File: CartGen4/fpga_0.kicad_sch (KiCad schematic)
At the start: 16 parts

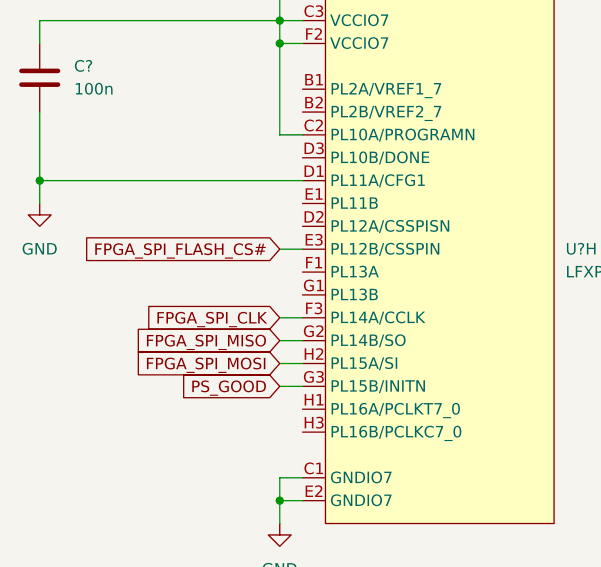
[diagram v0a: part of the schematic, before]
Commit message: Connected and fixed reset
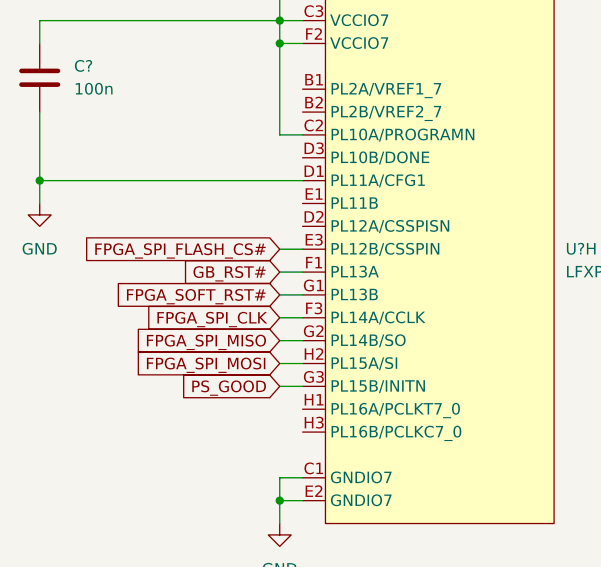
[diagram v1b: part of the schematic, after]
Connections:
- net GB_RST#: now reaches U?.F1 (PL13A)
- net FPGA_SOFT_RST#: now reaches U?.G1 (PL13B)
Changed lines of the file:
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@@
+    (stroke (width 0) (type default) (color 0 0 0 0))
+  )
+  (wire (pts (xy 53.34 74.93) (xy 55.88 74.93))
     (stroke (width 0) (type default) (color 0 0 0 0))
   )
@@
   )
   (wire (pts (xy 143.51 86.36) (xy 143.51 88.9))
+    (stroke (width 0) (type default) (color 0 0 0 0))
+  )
+  (wire (pts (xy 53.34 77.47) (xy 55.88 77.47))
     (stroke (width 0) (type default) (color 0 0 0 0))
   )
@@
     )
   )
+  (global_label "FPGA_SOFT_RST#" (shape input) (at 53.34 77.47 180) (fields_autoplaced)
+    (effects (font (size 1.27 1.27)) (justify right))
+    (property "Intersheet References" "${INTERSHEET_REFS}" (id 0) (at 34.9612 77.5494 0)
+      (effects (font (size 1.27 1.27)) (justify right) hide)
+    )
+  )
   (global_label "FPGA_SPI_CLK" (shape input) (at 53.34 80.01 180) (fields_autoplaced)
     (effects (font (size 1.27 1.27)) (justify right))
@@
       (effects (font (size 1.27 1.27)) (justify right) hide)
     )
+  )
+  (global_label "GB_RST#" (shape input) (at 53.34 74.93 180) (fields_autoplaced)
+    (effects (font (size 1.27 1.27)) (justify right))
+    (property "Intersheet References" "${INTERSHEET_REFS}" (id 0) (at 42.7021 75.0094 0)
+      (effects (font (size 1.27 1.27)) (justify right) hide)
+    )

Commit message: Added copyright
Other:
- company: (none) -> © Elijah Almeida Coimbra
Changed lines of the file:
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@@
   (title_block
     (title "FPGA connections 0")
+    (company "© Elijah Almeida Coimbra")
   )
   (junction (at 209.55 128.27) (diameter 0) (color 0 0 0 0)

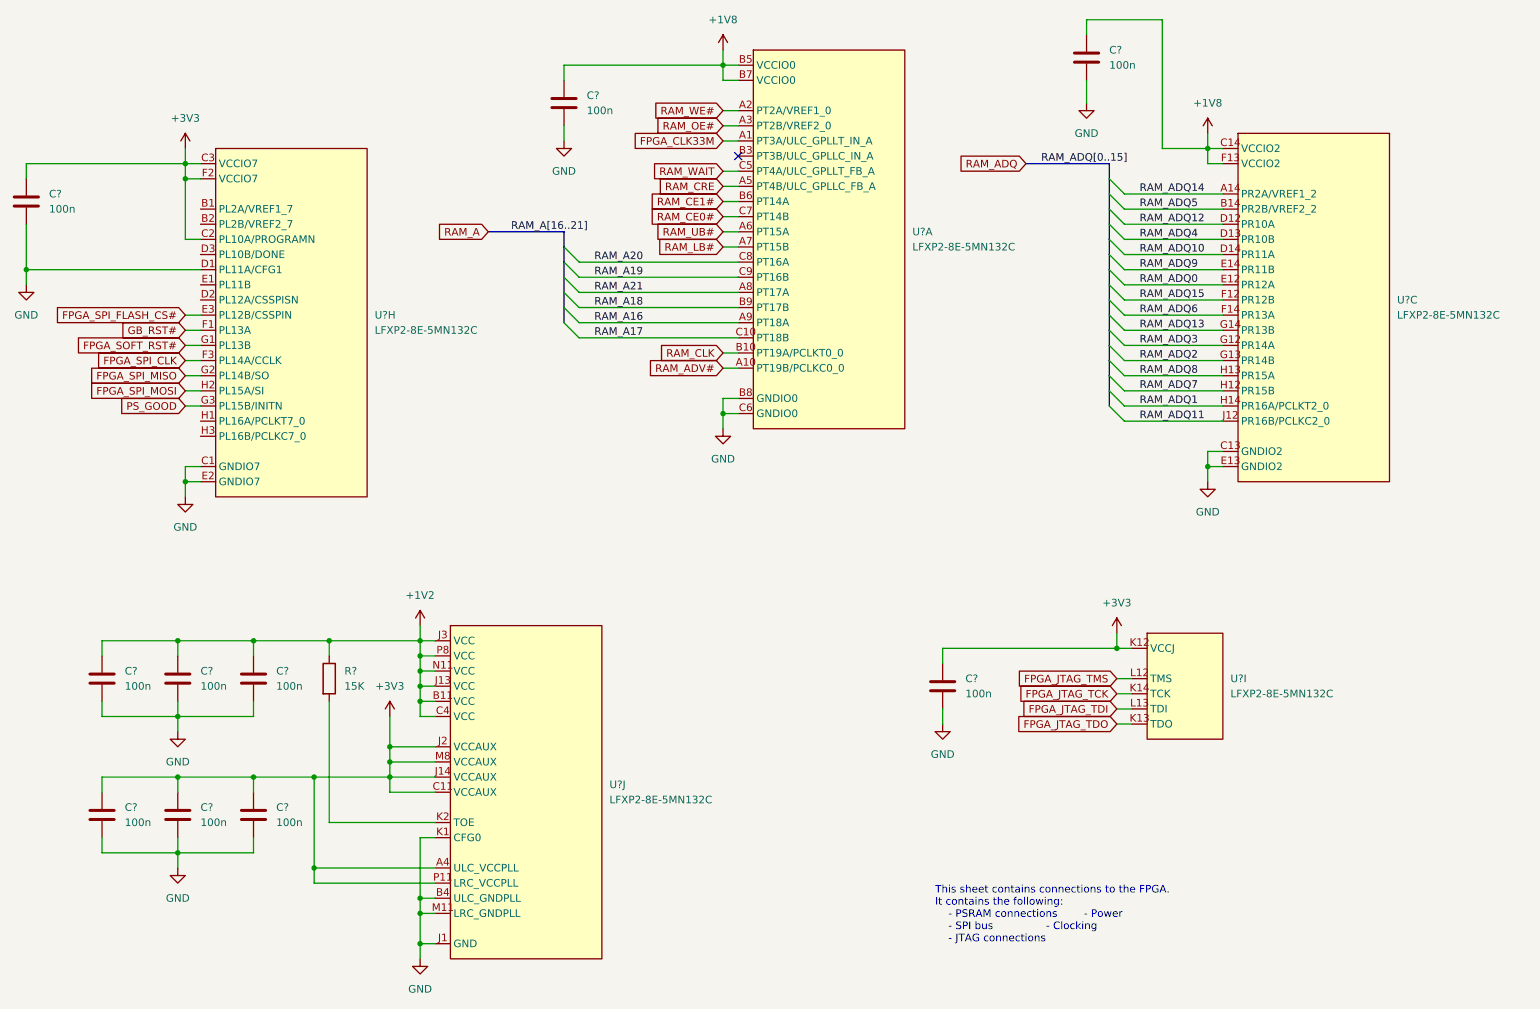
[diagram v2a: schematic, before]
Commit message: Added reference designators to everything
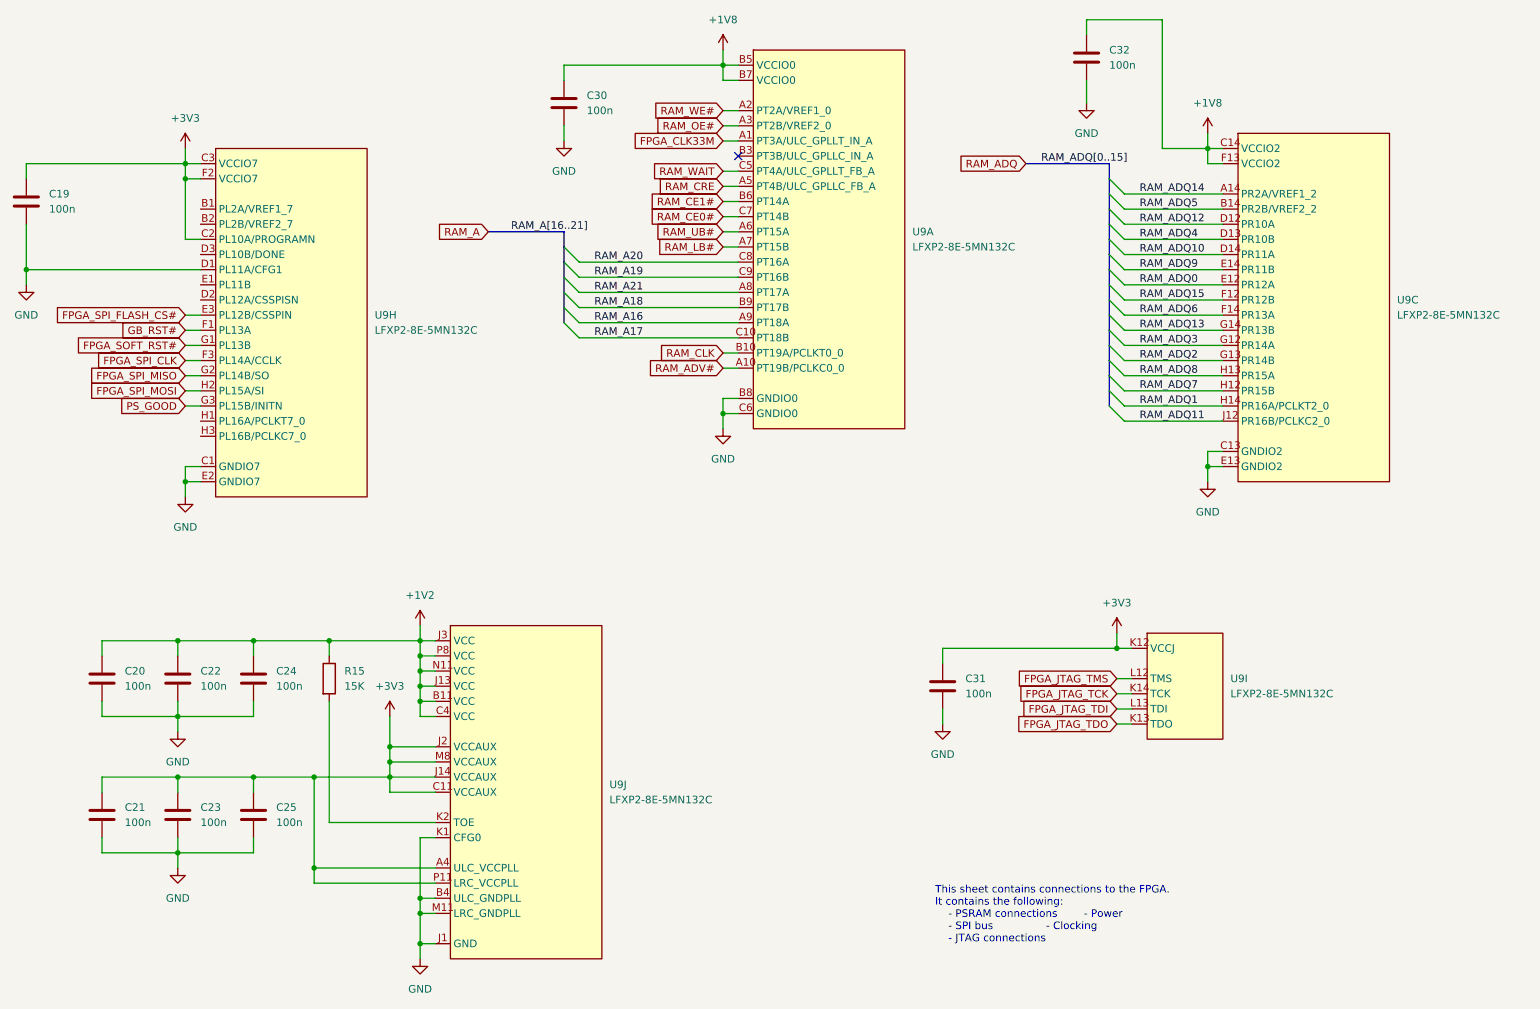
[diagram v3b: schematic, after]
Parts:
- gave numbers to parts that had none: 12
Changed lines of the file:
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@@
   (symbol (lib_id "Device:C") (at 204.47 29.21 0) (unit 1)
     (in_bom yes) (on_board yes) (fields_autoplaced)
-    (property "Reference" "C?" (id 0) (at 208.28 27.9399 0)
+    (property "Reference" "C32" (id 0) (at 208.28 27.9399 0)
       (effects (font (size 1.27 1.27)) (justify left))
     )
@@
   (symbol (lib_id "power:GND") (at 53.34 102.87 0) (unit 1)
     (in_bom yes) (on_board yes) (fields_autoplaced)
-    (property "Reference" "#PWR?" (id 0) (at 53.34 109.22 0)
+    (property "Reference" "#PWR061" (id 0) (at 53.34 109.22 0)
       (effects (font (size 1.27 1.27)) hide)
     )
@@
   (symbol (lib_id "power:+3V3") (at 53.34 44.45 0) (unit 1)
     (in_bom yes) (on_board yes) (fields_autoplaced)
-    (property "Reference" "#PWR?" (id 0) (at 53.34 48.26 0)
+    (property "Reference" "#PWR060" (id 0) (at 53.34 48.26 0)
       (effects (font (size 1.27 1.27)) hide)
     )
@@
   (symbol (lib_id "power:GND") (at 52.07 142.24 0) (unit 1)
     (in_bom yes) (on_board yes) (fields_autoplaced)
-    (property "Reference" "#PWR?" (id 0) (at 52.07 148.59 0)
+    (property "Reference" "#PWR058" (id 0) (at 52.07 148.59 0)
       (effects (font (size 1.27 1.27)) hide)
     )
@@
   (symbol (lib_id "power:GND") (at 143.51 91.44 0) (unit 1)
     (in_bom yes) (on_board yes)
-    (property "Reference" "#PWR?" (id 0) (at 143.51 97.79 0)
+    (property "Reference" "#PWR067" (id 0) (at 143.51 97.79 0)
       (effects (font (size 1.27 1.27)) hide)
     )
@@
   (symbol (lib_id "power:+3V3") (at 209.55 125.73 0) (unit 1)
     (in_bom yes) (on_board yes) (fields_autoplaced)
-    (property "Reference" "#PWR?" (id 0) (at 209.55 129.54 0)
+    (property "Reference" "#PWR070" (id 0) (at 209.55 129.54 0)
       (effects (font (size 1.27 1.27)) hide)
     )
@@
   (symbol (lib_id "power:+3V3") (at 87.63 139.7 0) (unit 1)
     (in_bom yes) (on_board yes) (fields_autoplaced)
-    (property "Reference" "#PWR?" (id 0) (at 87.63 143.51 0)
+    (property "Reference" "#PWR062" (id 0) (at 87.63 143.51 0)
       (effects (font (size 1.27 1.27)) hide)
     )
@@
   (symbol (lib_id "FPGA_Lattice:LFXP2-8E-5MN132C") (at 97.79 124.46 0) (unit 10)
     (in_bom yes) (on_board yes) (fields_autoplaced)
-    (property "Reference" "U?" (id 0) (at 124.46 151.1299 0)
+    (property "Reference" "U9" (id 0) (at 124.46 151.1299 0)
       (effects (font (size 1.27 1.27)) (justify left))
     )
@@
   (symbol (lib_id "FPGA_Lattice:LFXP2-8E-5MN132C") (at 58.42 44.45 0) (unit 8)
     (in_bom yes) (on_board yes) (fields_autoplaced)
-    (property "Reference" "U?" (id 0) (at 85.09 72.3899 0)
+    (property "Reference" "U9" (id 0) (at 85.09 72.3899 0)
       (effects (font (size 1.27 1.27)) (justify left))
     )
@@
   (symbol (lib_id "power:GND") (at 92.71 180.34 0) (unit 1)
     (in_bom yes) (on_board yes) (fields_autoplaced)
-    (property "Reference" "#PWR?" (id 0) (at 92.71 186.69 0)
+    (property "Reference" "#PWR064" (id 0) (at 92.71 186.69 0)
       (effects (font (size 1.27 1.27)) hide)
     )
@@
   (symbol (lib_id "FPGA_Lattice:LFXP2-8E-5MN132C") (at 148.59 27.94 0) (unit 1)
     (in_bom yes) (on_board yes) (fields_autoplaced)
-    (property "Reference" "U?" (id 0) (at 175.26 58.4199 0)
+    (property "Reference" "U9" (id 0) (at 175.26 58.4199 0)
       (effects (font (size 1.27 1.27)) (justify left))
     )
@@
   (symbol (lib_id "power:+1V8") (at 224.79 41.91 0) (unit 1)
     (in_bom yes) (on_board yes)
-    (property "Reference" "#PWR?" (id 0) (at 224.79 45.72 0)
+    (property "Reference" "#PWR071" (id 0) (at 224.79 45.72 0)
       (effects (font (size 1.27 1.27)) hide)
     )
@@
   (symbol (lib_id "power:GND") (at 224.79 100.33 0) (unit 1)
     (in_bom yes) (on_board yes)
-    (property "Reference" "#PWR?" (id 0) (at 224.79 106.68 0)
+    (property "Reference" "#PWR072" (id 0) (at 224.79 106.68 0)
       (effects (font (size 1.27 1.27)) hide)
     )
@@
   (symbol (lib_id "Device:C") (at 39.37 156.21 0) (unit 1)
     (in_bom yes) (on_board yes) (fields_autoplaced)
-    (property "Reference" "C?" (id 0) (at 43.18 154.9399 0)
+    (property "Reference" "C21" (id 0) (at 43.18 154.9399 0)
       (effects (font (size 1.27 1.27)) (justify left))
     )
@@
   (symbol (lib_id "power:+1V8") (at 143.51 27.94 0) (unit 1)
     (in_bom yes) (on_board yes) (fields_autoplaced)
-    (property "Reference" "#PWR?" (id 0) (at 143.51 31.75 0)
+    (property "Reference" "#PWR066" (id 0) (at 143.51 31.75 0)
       (effects (font (size 1.27 1.27)) hide)
     )
@@
   (symbol (lib_id "Device:C") (at 116.84 36.83 0) (unit 1)
     (in_bom yes) (on_board yes) (fields_autoplaced)
-    (property "Reference" "C?" (id 0) (at 120.65 35.5599 0)
+    (property "Reference" "C30" (id 0) (at 120.65 35.5599 0)
       (effects (font (size 1.27 1.27)) (justify left))
     )
@@
   (symbol (lib_id "Device:R") (at 77.47 133.35 0) (unit 1)
     (in_bom yes) (on_board yes) (fields_autoplaced)
-    (property "Reference" "R?" (id 0) (at 80.01 132.0799 0)
+    (property "Reference" "R15" (id 0) (at 80.01 132.0799 0)
       (effects (font (size 1.27 1.27)) (justify left))
     )
@@
   (symbol (lib_id "power:GND") (at 26.67 67.31 0) (unit 1)
     (in_bom yes) (on_board yes) (fields_autoplaced)
-    (property "Reference" "#PWR?" (id 0) (at 26.67 73.66 0)
+    (property "Reference" "#PWR057" (id 0) (at 26.67 73.66 0)
       (effects (font (size 1.27 1.27)) hide)
     )
@@
   (symbol (lib_id "power:GND") (at 204.47 36.83 0) (unit 1)
     (in_bom yes) (on_board yes) (fields_autoplaced)
-    (property "Reference" "#PWR?" (id 0) (at 204.47 43.18 0)
+    (property "Reference" "#PWR069" (id 0) (at 204.47 43.18 0)
       (effects (font (size 1.27 1.27)) hide)
     )
@@
   (symbol (lib_id "Device:C") (at 180.34 134.62 0) (unit 1)
     (in_bom yes) (on_board yes) (fields_autoplaced)
-    (property "Reference" "C?" (id 0) (at 184.15 133.3499 0)
+    (property "Reference" "C31" (id 0) (at 184.15 133.3499 0)
       (effects (font (size 1.27 1.27)) (justify left))
     )
@@
   (symbol (lib_id "Device:C") (at 64.77 133.35 0) (unit 1)
     (in_bom yes) (on_board yes) (fields_autoplaced)
-    (property "Reference" "C?" (id 0) (at 68.58 132.0799 0)
+    (property "Reference" "C24" (id 0) (at 68.58 132.0799 0)
       (effects (font (size 1.27 1.27)) (justify left))
     )
@@
   (symbol (lib_id "power:GND") (at 180.34 140.97 0) (unit 1)
     (in_bom yes) (on_board yes) (fields_autoplaced)
-    (property "Reference" "#PWR?" (id 0) (at 180.34 147.32 0)
+    (property "Reference" "#PWR068" (id 0) (at 180.34 147.32 0)
       (effects (font (size 1.27 1.27)) hide)
     )
@@
   (symbol (lib_id "power:+1V2") (at 92.71 124.46 0) (unit 1)
     (in_bom yes) (on_board yes) (fields_autoplaced)
-    (property "Reference" "#PWR?" (id 0) (at 92.71 128.27 0)
+    (property "Reference" "#PWR063" (id 0) (at 92.71 128.27 0)
       (effects (font (size 1.27 1.27)) hide)
     )
@@
   (symbol (lib_id "FPGA_Lattice:LFXP2-8E-5MN132C") (at 214.63 125.73 0) (unit 9)
     (in_bom yes) (on_board yes) (fields_autoplaced)
-    (property "Reference" "U?" (id 0) (at 228.6 133.3499 0)
+    (property "Reference" "U9" (id 0) (at 228.6 133.3499 0)
       (effects (font (size 1.27 1.27)) (justify left))
     )
@@
   (symbol (lib_id "Device:C") (at 52.07 133.35 0) (unit 1)
     (in_bom yes) (on_board yes) (fields_autoplaced)
-    (property "Reference" "C?" (id 0) (at 55.88 132.0799 0)
+    (property "Reference" "C22" (id 0) (at 55.88 132.0799 0)
       (effects (font (size 1.27 1.27)) (justify left))
     )
@@
   (symbol (lib_id "Device:C") (at 26.67 53.34 0) (unit 1)
     (in_bom yes) (on_board yes) (fields_autoplaced)
-    (property "Reference" "C?" (id 0) (at 30.48 52.0699 0)
+    (property "Reference" "C19" (id 0) (at 30.48 52.0699 0)
       (effects (font (size 1.27 1.27)) (justify left))
     )
@@
   (symbol (lib_id "power:GND") (at 116.84 43.18 0) (unit 1)
     (in_bom yes) (on_board yes) (fields_autoplaced)
-    (property "Reference" "#PWR?" (id 0) (at 116.84 49.53 0)
+    (property "Reference" "#PWR065" (id 0) (at 116.84 49.53 0)
       (effects (font (size 1.27 1.27)) hide)
     )
@@
   (symbol (lib_id "Device:C") (at 39.37 133.35 0) (unit 1)
     (in_bom yes) (on_board yes) (fields_autoplaced)
-    (property "Reference" "C?" (id 0) (at 43.18 132.0799 0)
+    (property "Reference" "C20" (id 0) (at 43.18 132.0799 0)
       (effects (font (size 1.27 1.27)) (justify left))
     )
@@
   (symbol (lib_id "FPGA_Lattice:LFXP2-8E-5MN132C") (at 229.87 41.91 0) (unit 3)
     (in_bom yes) (on_board yes) (fields_autoplaced)
-    (property "Reference" "U?" (id 0) (at 256.54 69.8499 0)
+    (property "Reference" "U9" (id 0) (at 256.54 69.8499 0)
       (effects (font (size 1.27 1.27)) (justify left))
     )
@@
   (symbol (lib_id "Device:C") (at 52.07 156.21 0) (unit 1)
     (in_bom yes) (on_board yes) (fields_autoplaced)
-    (property "Reference" "C?" (id 0) (at 55.88 154.9399 0)
+    (property "Reference" "C23" (id 0) (at 55.88 154.9399 0)
       (effects (font (size 1.27 1.27)) (justify left))
     )
@@
   (symbol (lib_id "Device:C") (at 64.77 156.21 0) (unit 1)
     (in_bom yes) (on_board yes) (fields_autoplaced)
-    (property "Reference" "C?" (id 0) (at 68.58 154.9399 0)
+    (property "Reference" "C25" (id 0) (at 68.58 154.9399 0)
       (effects (font (size 1.27 1.27)) (justify left))
     )
@@
   (symbol (lib_id "power:GND") (at 52.07 165.1 0) (unit 1)
     (in_bom yes) (on_board yes) (fields_autoplaced)
-    (property "Reference" "#PWR?" (id 0) (at 52.07 171.45 0)
-      (effects (font (size 1.27 1.27)) hide)
-    )
+    (property "Reference" "#PWR059" (id 0) (at 52.07 171.45 0)
+      (effects (font (size 1.27 1.27)) hide)
+    )

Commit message: Fixed DRC
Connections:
- net PS_GOOD renamed PS_PGOOD
- no-connect marks 1 -> 8
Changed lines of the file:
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@@
   )
   (no_connect (at 146.05 45.72))
+  (no_connect (at 55.88 54.61))
+  (no_connect (at 55.88 57.15))
+  (no_connect (at 55.88 62.23))
+  (no_connect (at 55.88 69.85))
+  (no_connect (at 55.88 67.31))
+  (no_connect (at 55.88 92.71))
+  (no_connect (at 55.88 90.17))
   (bus_entry (at 208.28 77.47) (size 2.54 2.54)
     (stroke (width 0) (type default) (color 0 0 0 0))
@@
     )
   )
-  (global_label "RAM_ADQ" (shape input) (at 194.31 46.99 180) (fields_autoplaced)
-    (effects (font (size 1.27 1.27)) (justify right))
-    (property "Intersheet References" "${INTERSHEET_REFS}" (id 0) (at 183.4302 47.0694 0)
+  (global_label "RAM_ADQ[0..15]" (shape input) (at 194.31 46.99 180) (fields_autoplaced)
+    (effects (font (size 1.27 1.27)) (justify right))
+    (property "Intersheet References" "${INTERSHEET_REFS}" (id 0) (at 176.8988 46.9106 0)
       (effects (font (size 1.27 1.27)) (justify right) hide)
     )
@@
     )
   )
-  (global_label "PS_GOOD" (shape input) (at 53.34 87.63 180) (fields_autoplaced)
-    (effects (font (size 1.27 1.27)) (justify right))
-    (property "Intersheet References" "${INTERSHEET_REFS}" (id 0) (at 42.2788 87.5506 0)
+  (global_label "PS_PGOOD" (shape input) (at 53.34 87.63 180) (fields_autoplaced)
+    (effects (font (size 1.27 1.27)) (justify right))
+    (property "Intersheet References" "${INTERSHEET_REFS}" (id 0) (at 41.0088 87.5506 0)
       (effects (font (size 1.27 1.27)) (justify right) hide)
     )
@@
     )
   )
-  (global_label "RAM_A" (shape input) (at 104.14 58.42 180) (fields_autoplaced)
-    (effects (font (size 1.27 1.27)) (justify right))
-    (property "Intersheet References" "${INTERSHEET_REFS}" (id 0) (at 95.8607 58.4994 0)
-      (effects (font (size 1.27 1.27)) (justify right) hide)
-    )
+  (global_label "RAM_A[16..21]" (shape input) (at 104.14 58.42 180) (fields_autoplaced)
+    (effects (font (size 1.27 1.27)) (justify right))
+    (property "Intersheet References" "${INTERSHEET_REFS}" (id 0) (at 88.1198 58.3406 0)
+      (effects (font (size 1.27 1.27)) (justify right) hide)
+    )
